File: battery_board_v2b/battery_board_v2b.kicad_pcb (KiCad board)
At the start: 4 copper layers, 88 x 94.5 mm, 137 parts, among them IC1 PCA9685PW,118, IC2 LT3652IMSE#PBF, IC3 PCT2075DP,118, J1 Face0, J11 CHARGE, J12 Foot0, J13 Foot1, J14 Foot2, J15 Foot3, J16 RBF, J17 BURN, J18 Bypass, J19 Heater, J2 Face1, J3 Face2, J4 Face3, J6 FC_FACE, J7 5V Breakout, J8 ISS, J9 TC, K1 APAN3105, Q1 IRF7458, Q2 IRF7458, Q3 MBT2222ADW1T1, Q4 MBT2222ADW1T1, Q5 IRLML2803, Q6 NDS8434, Q7 MMBT2222AT, Q8 IRLML2803, Q9 NDS8434, U1 R5460N208AA, U10 TLVH431 DBZ SOT-23, U11 ADS1015IDGS, U2 TPS54226PWPRPWP14_2P31X2P46-L, U3 INA219AxD, U4 TCA9548APWR, U5 TPS7A4501DCQT, U6 INA219AxD, U7 1049, U8 1049, U9 AD8495

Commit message: Update BOM with part numbers and replace obsolete parts
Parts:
- Q6, Q9: value NDS8434 -> SQ4401CEY-T1_GE3
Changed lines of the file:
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@@
 			)
 		)
-		(property "Value" "NDS8434"
+		(property "Value" "SQ4401CEY-T1_GE3"
 			(at -0.254493 0.432628 90)
 			(layer "F.SilkS")
@@
 			)
 		)
-		(property "Flight" "NDS8434"
+		(property "Flight" "SQ4401CEY-T1_GE3"
 			(at 200.582 -61.546 0)
 			(layer "F.Fab")
@@
 			)
 		)
-		(property "Manufacturer_Name" "ON Semiconductor"
+		(property "Manufacturer_Name" "Vishay Siliconix"
 			(at 200.582 -61.546 0)
 			(layer "F.Fab")
@@
 			)
 		)
-		(property "Manufacturer_Part_Number" "NDS8434"
+		(property "Manufacturer_Part_Number" "SQ4401CEY-T1_GE3"
 			(at 200.582 -61.546 0)
 			(layer "F.Fab")
@@
 			)
 		)
-		(property "Value" "NDS8434"
+		(property "Value" "SQ4401CEY-T1_GE3"
 			(at -0.254493 0.432628 90)
 			(layer "F.SilkS")
@@
 			)
 		)
-		(property "Flight" "NDS8434"
+		(property "Flight" "SQ4401CEY-T1_GE3"
 			(at 209.918899 -53.078899 0)
 			(layer "F.Fab")
@@
 			)
 		)
-		(property "Manufacturer_Name" "ON Semiconductor"
+		(property "Manufacturer_Name" "Vishay Siliconix"
 			(at 209.918899 -53.078899 0)
 			(layer "F.Fab")
@@
 			)
 		)
-		(property "Manufacturer_Part_Number" "NDS8434"
+		(property "Manufacturer_Part_Number" "SQ4401CEY-T1_GE3"
 			(at 209.918899 -53.078899 0)
 			(layer "F.Fab")

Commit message: Updated BOM to reflect parts availability
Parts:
- R33: value 85k -> 85.6k
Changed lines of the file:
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@@
 			)
 		)
-		(property "Value" "85k"
+		(property "Value" "85.6k"
 			(at 0 1.43 0)
 			(layer "F.Fab")

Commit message: Reliability Improvements
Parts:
- removed C13, C19: 200uF, Capacitor_SMD:C_1210_3225Metric
- J8: value ISS -> ISS Foot
- J9: value TC -> Thermocouple
- Q6, Q9: value SQ4401CEY-T1_GE3 -> NDS8434
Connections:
- J8 pad 2: PACK- -> B-
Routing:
- net B-: track 28.3 -> 102.0 mm
- net PACK-: track 73.6 -> 0.00 mm
- net GND: track 270.0 -> 260.8 mm
- net F2_ENB: track 96.4 -> 99.8 mm

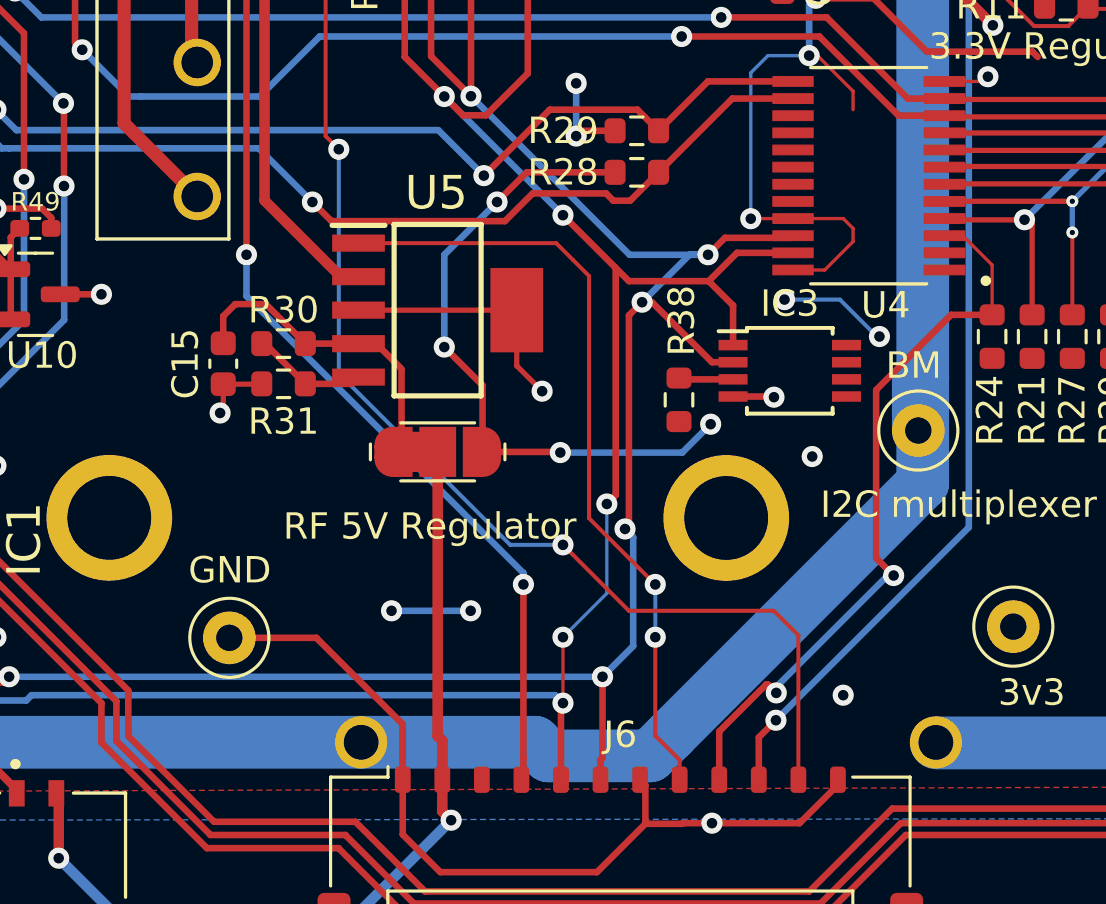
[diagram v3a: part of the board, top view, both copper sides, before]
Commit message: Changed the 5V buck converter to a more efficient one
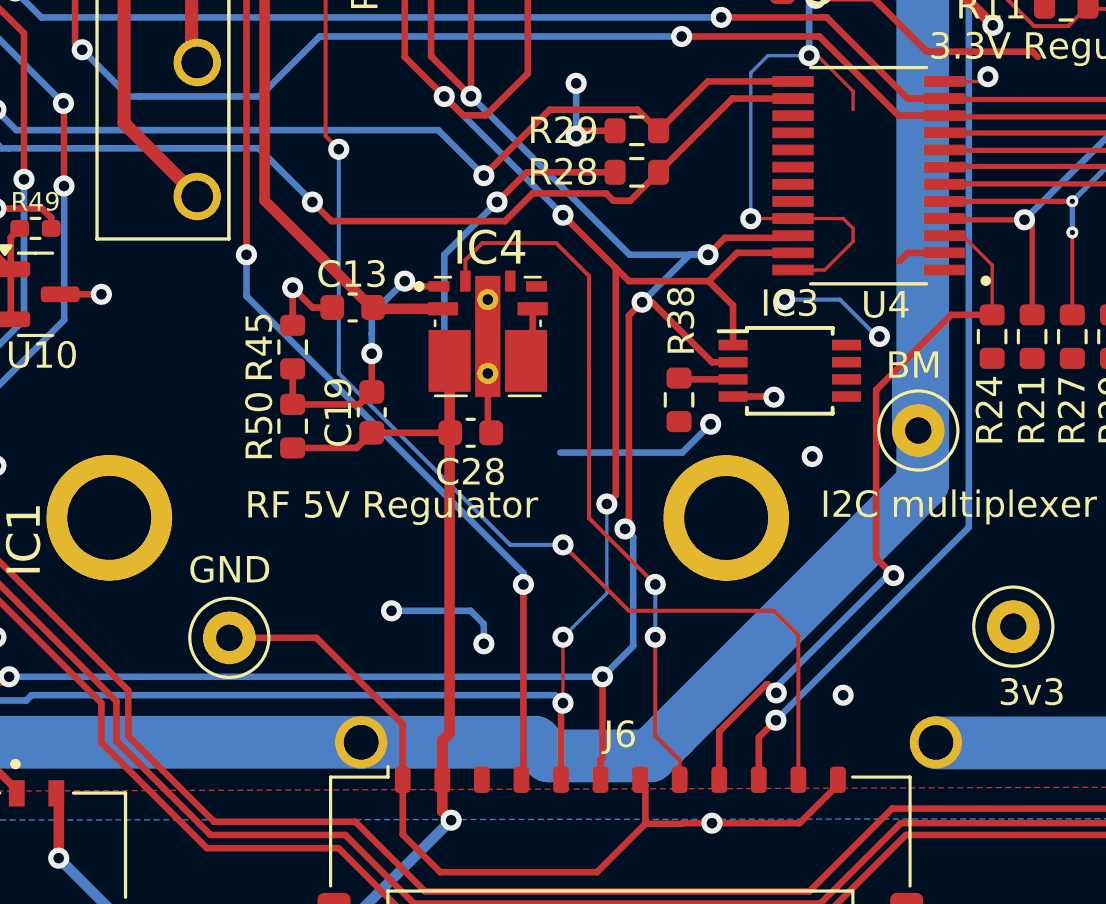
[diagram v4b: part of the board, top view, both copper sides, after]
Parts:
- removed C15: 10uF, Capacitor_SMD:C_0603_1608Metric
- removed JP1: Jumper_3_Bridged12, MaxLib:SolderJumper-3_P1.3mm_Bridged12_RoundedPad1.0x1.5mm
- removed R30: 10K, Resistor_SMD:R_0603_1608Metric
- removed R31: 3.3K, Resistor_SMD:R_0603_1608Metric
- removed U5: TPS7A4501DCQT, MaxLib:TPS7A4501DCQT
- added C13: 10uF, Capacitor_SMD:C_0603_1608Metric, F.Cu at (143.5, 109.0)
- added C19: 330pF / 38mOhm, Capacitor_SMD:C_0603_1608Metric, F.Cu at (144.2, 113.0)
- added C28: 47uF / 2.082mOhm, Capacitor_SMD:C_0603_1608Metric, F.Cu at (148.0, 113.8)
- added IC4: TPSM84209RKHT, TPSM84209RKHT:TPSM84209RKHT, F.Cu at (148.7, 110.1)
- added R45: 1.37kOhm, Resistor_SMD:R_0603_1608Metric, F.Cu at (141.2, 110.5)
- added R50: 10K, Resistor_SMD:R_0603_1608Metric, F.Cu at (141.2, 113.5)
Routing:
- net /V_RF: track 12.2 -> 0.00 mm
- net Net-(IC4-FB): track 0.00 -> 10.6 mm, vias 0 -> 2
- net VCC_RF1: track 34.0 -> 43.7 mm
- net GND: track 260.8 -> 255.7 mm, vias 60 -> 59
- net Net-(U5-SENSE/ADJ): track 4.40 -> 0.00 mm
- net VBUSP: track 172.0 -> 176.3 mm
- net +3V3: track 136.1 -> 131.9 mm, vias 22 -> 20
- net ENAB_RF: track 29.8 -> 26.8 mm
- net Net-(IC4-SW_1): track 0.00 -> 2.08 mm

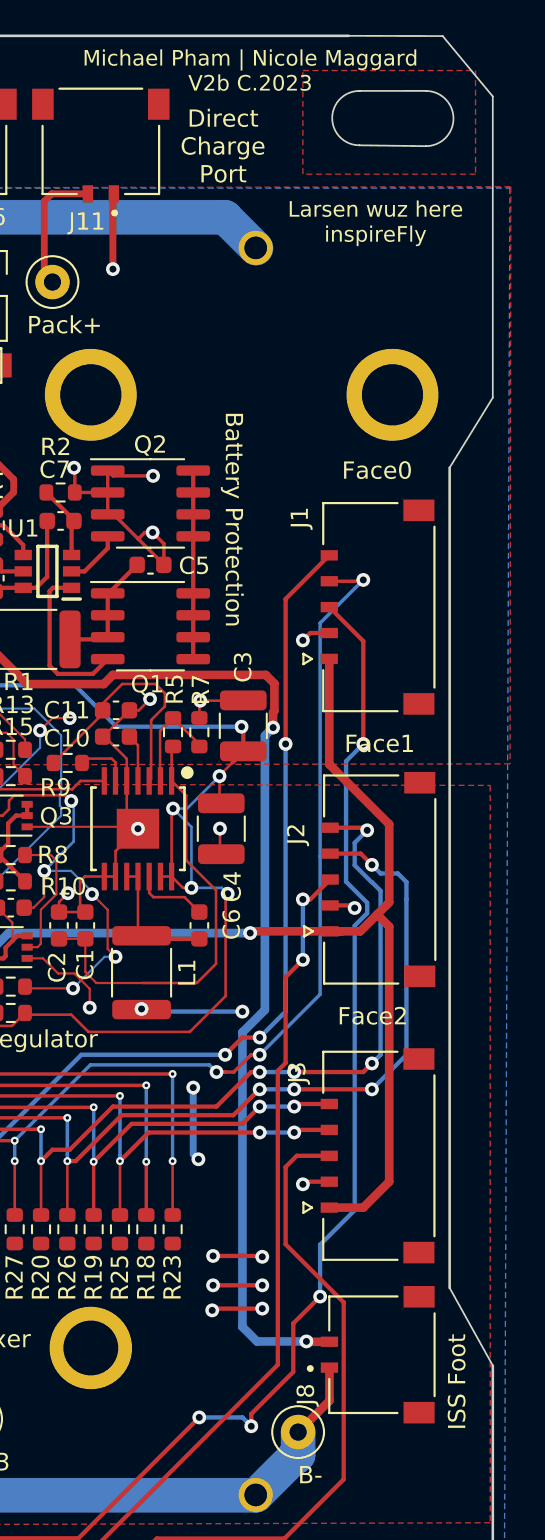
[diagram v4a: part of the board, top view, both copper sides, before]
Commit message: Updated 5v reg and lowside switch
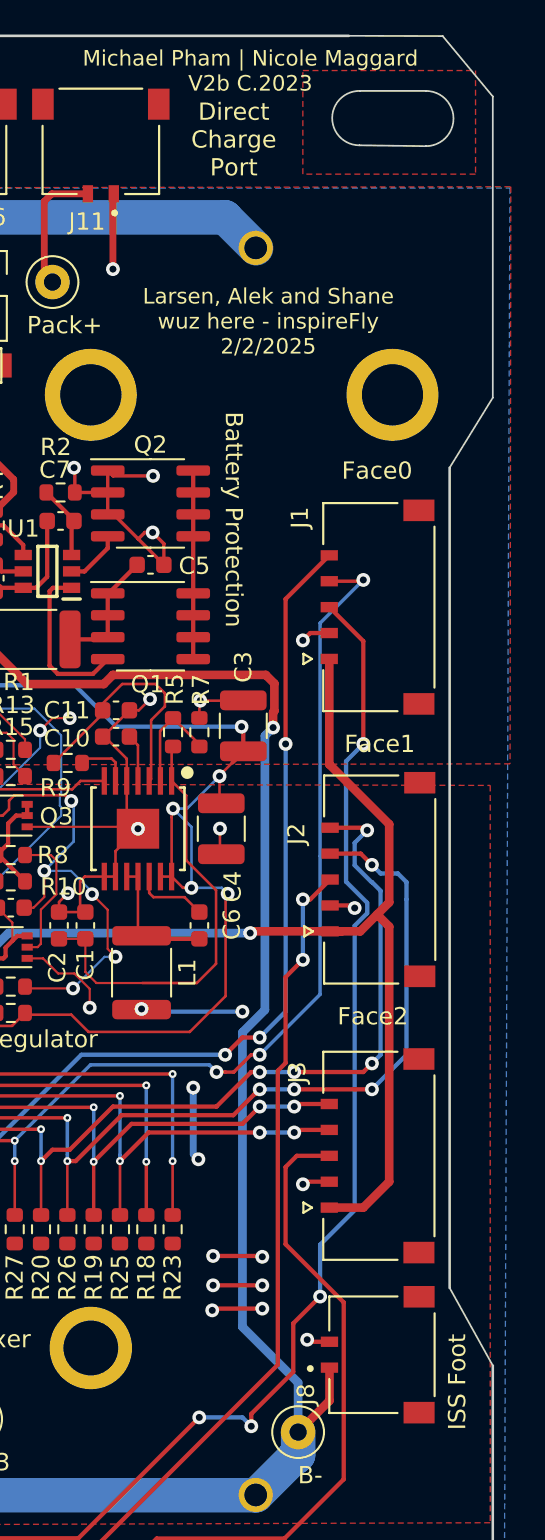
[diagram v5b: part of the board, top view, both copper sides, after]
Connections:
- J8 pad 2: B- -> GND
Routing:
- net B-: track 102.0 -> 104.0 mm, vias 2 -> 1
- net GND: track 255.7 -> 257.0 mm, vias 59 -> 60
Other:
- board text added: "Larsen, Alek and Shane wuz here - inspireFly 2/2/2025"
- board text removed: "Larsen wuz here inspireFly"
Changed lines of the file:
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@@
 			)
 		)
-		(property "Footprint" ""
+		(property "Footprint" "MOLEX PICO LOCK 2 POS:MOLEX_504050-0291"
 			(at 0 0 0)
 			(layer "F.Fab")
@@
 			(size 0.6 1)
 			(layers "F.Cu" "F.Paste" "F.Mask")
-			(net 7 "B-")
+			(net 16 "GND")
 			(pinfunction "Pin_2")
 			(pintype "passive")
@@
 			)
 		)
-		(property "Footprint" ""
+		(property "Footprint" "MOLEX PICO LOCK 2 POS:MOLEX_504050-0291"
 			(at 0 0 90)
 			(layer "F.Fab")
@@
 		(tags "capacitor")
 		(property "Reference" "C13"
-			(at 0.025 1.25 360)
+			(at 0.025 1.25 0)
 			(layer "F.SilkS")
 			(effects
@@
 		)
 		(property "Value" "10uF"
-			(at 0 1.43 360)
+			(at 0 1.43 0)
 			(layer "F.Fab")
 			(effects
@@
 		)
 		(fp_text user "${REFERENCE}"
-			(at 0 0 360)
+			(at 0 0 0)
 			(layer "F.Fab")
 			(effects
@@
 		)
 	)
-	(gr_text "Larsen wuz here\ninspireFly\n"
-		(at 191.705 51.77 0)
+	(gr_text "Larsen, Alek and Shane \nwuz here - inspireFly\n2/2/2025\n\n"
+		(at 185.5 58.25 0)
 		(layer "F.SilkS")
 		(effects
@@
 	)
 	(gr_text "Direct \nCharge \nPort"
-		(at 182.875 47.4 0)
+		(at 183.5 47 0)
 		(layer "F.SilkS")
 		(effects
@@
 	)
 	(segment
-		(start 187.9 116.62)
-		(end 187.88 116.6)
-		(width 0.5)
-		(layer "F.Cu")
-		(net 7)
-	)
-	(segment
-		(start 189.04 116.62)
-		(end 187.9 116.62)
-		(width 0.5)
-		(layer "F.Cu")
-		(net 7)
-	)
-	(segment
 		(start 168.943 75.943)
 		(end 168.0925 75.943)
@@
 		(net 7)
 	)
-	(via
-		(at 187.706 116.6)
-		(size 0.8)
-		(drill 0.4)
-		(layers "F.Cu" "B.Cu")
+	(segment
+		(start 187 123.3)
+		(end 187.1 123.3)
+		(width 2)
+		(layer "B.Cu")
 		(net 7)
 	)
 	(segment
-		(start 184 115.76)
-		(end 184 98.702082)
+		(start 185.3024 97.399682)
+		(end 185.3024 81.5231)
 		(width 0.5)
 		(layer "B.Cu")
@@
 	)
 	(segment
-		(start 187 123.3)
-		(end 187.1 123.3)
-		(width 2)
+		(start 184 98.702082)
+		(end 185.3024 97.399682)
+		(width 0.5)
 		(layer "B.Cu")
 		(net 7)
@@
 	)
 	(segment
-		(start 184.84 116.6)
-		(end 184 115.76)
+		(start 187.225 121.85)
+		(end 187.225 118.985)
 		(width 0.5)
 		(layer "B.Cu")
@@
 	)
 	(segment
-		(start 184 98.702082)
-		(end 185.3024 97.399682)
-		(width 0.5)
-		(layer "B.Cu")
-		(net 7)
-	)
-	(segment
-		(start 185.3024 97.399682)
-		(end 185.3024 81.5231)
+		(start 184 115.76)
+		(end 184 98.702082)
 		(width 0.5)
 		(layer "B.Cu")
@@
 	)
 	(segment
-		(start 187.706 116.6)
-		(end 184.84 116.6)
+		(start 185.3024 81.5231)
+		(end 185.7755 81.05)
 		(width 0.5)
 		(layer "B.Cu")
@@
 	)
 	(segment
-		(start 185.3024 81.5231)
-		(end 185.7755 81.05)
+		(start 187.225 118.985)
+		(end 184 115.76)
 		(width 0.5)
 		(layer "B.Cu")
@@
 	)
 	(segment
-		(start 187.88 116.6)
-		(end 187.706 116.6)
-		(width 0.5)
-		(layer "B.Cu")
-		(net 7)
-	)
-	(segment
 		(start 174.106 69.222)
 		(end 174.243 69.085)
@@
 	)
 	(segment
+		(start 189.04 116.62)
+		(end 187.87 116.62)
+		(width 0.25)
+		(layer "F.Cu")
+		(net 16)
+	)
+	(segment
 		(start 187.925 75.575)
 		(end 187.5 76)
@@
 	)
 	(segment
+		(start 187.87 116.62)
+		(end 187.75 116.5)
+		(width 0.25)
+		(layer "F.Cu")
+		(net 16)
+	)
+	(segment
 		(start 141.402 57.9358)
 		(end 141.402 59.7006)
@@
 		(net 16)
 	)
+	(via
+		(at 187.75 116.5)
+		(size 0.8)
+		(drill 0.4)
+		(layers "F.Cu" "B.Cu")
+		(free yes)
+		(net 16)
+	)
